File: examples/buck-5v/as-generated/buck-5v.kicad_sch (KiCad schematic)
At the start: 18 parts, among them J1 12V IN, J2 5V OUT, U1 LM2596S-5

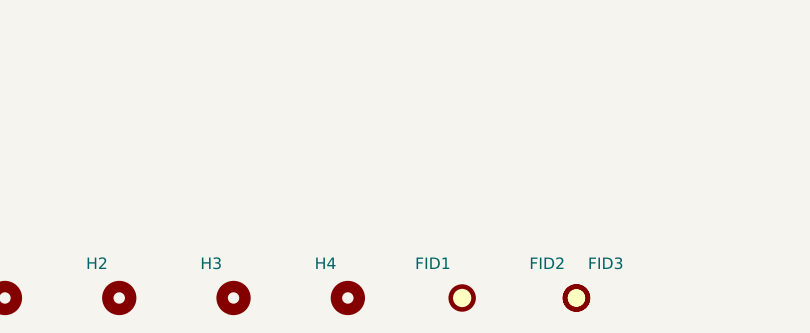
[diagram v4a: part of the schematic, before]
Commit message: Leave room for the screw, and print the ink where the board is
The screw holes were placed against the hole's own courtyard, which is the
drill plus a whisker - so on four of the five boards a hole sat inside a
connector's mating space, closest 0.42 mm. What goes through an M3 hole is a
pan head on a washer, seven millimetres of steel lying flat, and a connector
wants its shell, its wires and the fingers that fit them on top of that. The
spot search now keeps the fastener's own circle clear of every part body and
gives connectors CONNECTOR_ACCESS more, and three rules say so when a board
does not: mechanical.fastener_clearance, mechanical.connector_access and
mechanical.fastener_copper, all blocking for a generated design.

Silk was measured with a per-character advance of 0.78, and KiCad's stroke
font is proportional at 0.94 to 1.07. Everything downstream of that estimate
was placing ink where it did not fit: a legend across a capacitor's land, a
designator through the board's own name. `_text_extent` takes the top of the
measured range, adds the fab's clearance and is used by every silk placement.

Three placements also fell through to a position nobody chose. A designator
that found nothing kept its library offset, which for a part in a corner
points off the board; the board id took the first of eight fixed strips; a
legend took the least bad of six spots. All three are scored now, over
candidate sets wide enough to have an answer - and a pad-less footprint, which
is what a mounting hole is, is no longer skipped outright.

silk.off_board reports the case KiCad's own test cannot: ink that clears the
edge entirely is never printed, and DRC only measures ink that crosses it.

_unspiked redraws a corner tighter than a right angle as the elbow between its
neighbours - one diagonal, one straight, no step back to a heading the line
has already left. It is never longer than what it replaces.

All four fast boards: 0 errors, 0 warnings.

Co-Authored-By: Claude Fable 5 <no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
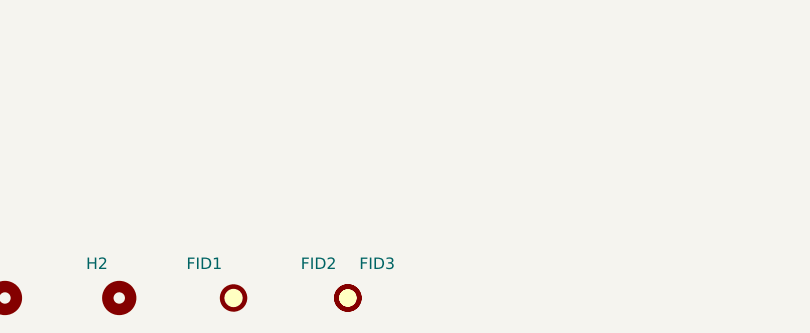
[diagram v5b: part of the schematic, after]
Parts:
- removed H3, H4: M3, MountingHole:MountingHole_3.2mm_M3, symbol Mechanical:MountingHole
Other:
- moved on the sheet: FID1, FID2, FID3
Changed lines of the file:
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@@
     (instances (project "buck-5v" (path "/ec98644d-848c-5056-a4cb-c829189be5c3" (reference "H2") (unit 1))))
   )
-  (symbol (lib_id "Mechanical:MountingHole") (at 51.11 149.67 0.0) (unit 1)
+  (symbol (lib_id "Mechanical:Fiducial") (at 51.11 149.67 0.0) (unit 1)
     (exclude_from_sim no) (in_bom no) (on_board yes) (dnp no)
-    (property "Reference" "H3" (at 49.84 145.86 0) (effects (font (size 1.27 1.27)) (justify right)))
-    (property "Value" "M3" (at 54.92 152.21 0) (effects (font (size 1.27 1.27)) (justify left) hide))
-    (property "Footprint" "MountingHole:MountingHole_3.2mm_M3" (at 51.11 149.67 0) (effects (font (size 1.27 1.27)) hide))
+    (property "Reference" "FID1" (at 49.84 145.86 0) (effects (font (size 1.27 1.27)) (justify right)))
+    (property "Value" "Fiducial" (at 54.92 152.21 0) (effects (font (size 1.27 1.27)) (justify left) hide))
+    (property "Footprint" "Fiducial:Fiducial_1mm_Mask2mm" (at 51.11 149.67 0) (effects (font (size 1.27 1.27)) hide))
     (property "Datasheet" "~" (at 51.11 149.67 0) (effects (font (size 1.27 1.27)) hide))
-    (instances (project "buck-5v" (path "/ec98644d-848c-5056-a4cb-c829189be5c3" (reference "H3") (unit 1))))
-  )
-  (symbol (lib_id "Mechanical:MountingHole") (at 63.81 149.67 0.0) (unit 1)
-    (exclude_from_sim no) (in_bom no) (on_board yes) (dnp no)
-    (property "Reference" "H4" (at 62.54 145.86 0) (effects (font (size 1.27 1.27)) (justify right)))
-    (property "Value" "M3" (at 67.62 152.21 0) (effects (font (size 1.27 1.27)) (justify left) hide))
-    (property "Footprint" "MountingHole:MountingHole_3.2mm_M3" (at 63.81 149.67 0) (effects (font (size 1.27 1.27)) hide))
-    (property "Datasheet" "~" (at 63.81 149.67 0) (effects (font (size 1.27 1.27)) hide))
-    (instances (project "buck-5v" (path "/ec98644d-848c-5056-a4cb-c829189be5c3" (reference "H4") (unit 1))))
-  )
-  (symbol (lib_id "Mechanical:Fiducial") (at 76.51 149.67 0.0) (unit 1)
-    (exclude_from_sim no) (in_bom no) (on_board yes) (dnp no)
-    (property "Reference" "FID1" (at 75.24 145.86 0) (effects (font (size 1.27 1.27)) (justify right)))
-    (property "Value" "Fiducial" (at 80.32 152.21 0) (effects (font (size 1.27 1.27)) (justify left) hide))
-    (property "Footprint" "Fiducial:Fiducial_1mm_Mask2mm" (at 76.51 149.67 0) (effects (font (size 1.27 1.27)) hide))
-    (property "Datasheet" "~" (at 76.51 149.67 0) (effects (font (size 1.27 1.27)) hide))
     (instances (project "buck-5v" (path "/ec98644d-848c-5056-a4cb-c829189be5c3" (reference "FID1") (unit 1))))
   )
-  (symbol (lib_id "Mechanical:Fiducial") (at 89.21 149.67 0.0) (unit 1)
+  (symbol (lib_id "Mechanical:Fiducial") (at 63.81 149.67 0.0) (unit 1)
     (exclude_from_sim no) (in_bom no) (on_board yes) (dnp no)
-    (property "Reference" "FID2" (at 87.94 145.86 0) (effects (font (size 1.27 1.27)) (justify right)))
-    (property "Value" "Fiducial" (at 93.02 152.21 0) (effects (font (size 1.27 1.27)) (justify left) hide))
-    (property "Footprint" "Fiducial:Fiducial_1mm_Mask2mm" (at 89.21 149.67 0) (effects (font (size 1.27 1.27)) hide))
-    (property "Datasheet" "~" (at 89.21 149.67 0) (effects (font (size 1.27 1.27)) hide))
+    (property "Reference" "FID2" (at 62.54 145.86 0) (effects (font (size 1.27 1.27)) (justify right)))
+    (property "Value" "Fiducial" (at 67.62 152.21 0) (effects (font (size 1.27 1.27)) (justify left) hide))
+    (property "Footprint" "Fiducial:Fiducial_1mm_Mask2mm" (at 63.81 149.67 0) (effects (font (size 1.27 1.27)) hide))
+    (property "Datasheet" "~" (at 63.81 149.67 0) (effects (font (size 1.27 1.27)) hide))
     (instances (project "buck-5v" (path "/ec98644d-848c-5056-a4cb-c829189be5c3" (reference "FID2") (unit 1))))
   )
-  (symbol (lib_id "Mechanical:Fiducial") (at 89.21 149.67 0.0) (unit 1)
+  (symbol (lib_id "Mechanical:Fiducial") (at 63.81 149.67 0.0) (unit 1)
     (exclude_from_sim no) (in_bom no) (on_board yes) (dnp no)
-    (property "Reference" "FID3" (at 90.48 145.86 0) (effects (font (size 1.27 1.27)) (justify left)))
-    (property "Value" "Fiducial" (at 90.48 154.75 0) (effects (font (size 1.27 1.27)) (justify left) hide))
-    (property "Footprint" "Fiducial:Fiducial_1mm_Mask2mm" (at 89.21 149.67 0) (effects (font (size 1.27 1.27)) hide))
-    (property "Datasheet" "~" (at 89.21 149.67 0) (effects (font (size 1.27 1.27)) hide))
+    (property "Reference" "FID3" (at 65.08 145.86 0) (effects (font (size 1.27 1.27)) (justify left)))
+    (property "Value" "Fiducial" (at 65.08 154.75 0) (effects (font (size 1.27 1.27)) (justify left) hide))
+    (property "Footprint" "Fiducial:Fiducial_1mm_Mask2mm" (at 63.81 149.67 0) (effects (font (size 1.27 1.27)) hide))
+    (property "Datasheet" "~" (at 63.81 149.67 0) (effects (font (size 1.27 1.27)) hide))
     (instances (project "buck-5v" (path "/ec98644d-848c-5056-a4cb-c829189be5c3" (reference "FID3") (unit 1))))
   )

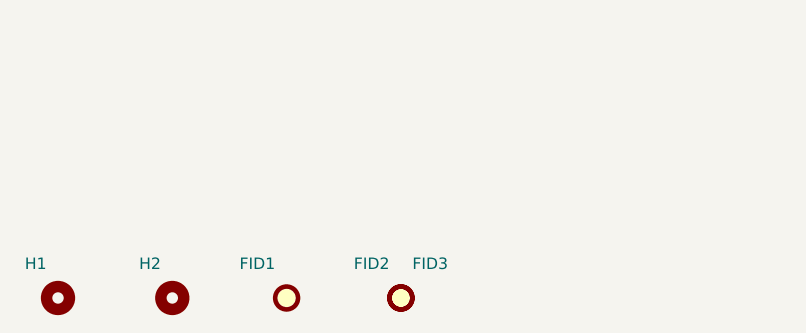
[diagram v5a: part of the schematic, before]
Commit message: Walk the whole edge for a screw hole, and land a joint on its own pad
The fastener clearance was right and the search was not: it slid along two
edges from each corner and gave up, so boards that had had four screw holes
came back with one. It now walks a ring round the board at the inset the
screw needs, taking the nearest free point to each corner - and only from
that corner's own quarter, because a search that asked for the nearest free
point anywhere put three of the four along one edge, each of them the nearest
thing to a different corner. A quarter with no room gives no screw: three
that hold the board flat beat four that hold one side.

A pin header asks for nothing above its courtyard - the socket that fits it
lands inside the outline the header already draws - while a screw terminal's
wires leave horizontally from its face. Treating the two alike is what left a
carrier lined with headers with two holes on one edge. Both the generator and
the rule now tell them apart by footprint.

_landed folds a via that sits beside a plated hole of its own net onto the
hole. The plating already joins the faces, so the via bought nothing and cost
hole-to-hole: two drills a millimetre apart leave 0.15 mm of laminate at a
0.25 mm rule, which is what DRC reported on the opamp board.

The fillets move to the end of the pipeline. A taper is built against the end
of a run, and _landed moves ends, so a teardrop laid before it pointed at
where the run used to stop - a nought-degree corner in the angle rule.

buck-5v, motor-driver, pico-carrier, opamp-filter: 0 errors, 0 warnings.

Co-Authored-By: Claude Fable 5 <noreply@anthropic.com>
Claude-Session: https://claude.ai/code/session_01DUj7Ltu92tWg159mCSacwY
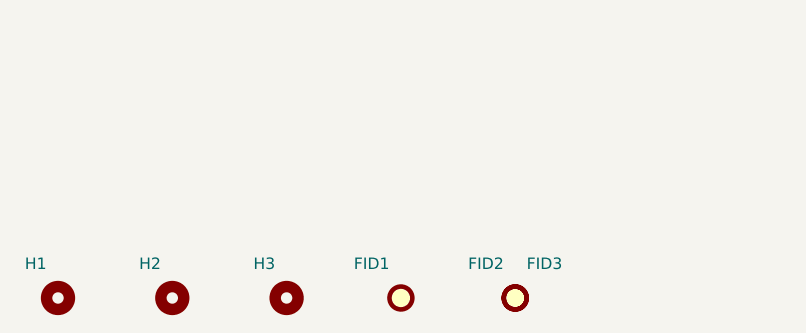
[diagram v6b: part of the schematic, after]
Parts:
- added H3: M3, MountingHole:MountingHole_3.2mm_M3, symbol Mechanical:MountingHole
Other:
- moved on the sheet: FID1, FID2, FID3
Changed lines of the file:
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@@
     (instances (project "buck-5v" (path "/ec98644d-848c-5056-a4cb-c829189be5c3" (reference "H2") (unit 1))))
   )
-  (symbol (lib_id "Mechanical:Fiducial") (at 51.11 149.67 0.0) (unit 1)
+  (symbol (lib_id "Mechanical:MountingHole") (at 51.11 149.67 0.0) (unit 1)
     (exclude_from_sim no) (in_bom no) (on_board yes) (dnp no)
-    (property "Reference" "FID1" (at 49.84 145.86 0) (effects (font (size 1.27 1.27)) (justify right)))
-    (property "Value" "Fiducial" (at 54.92 152.21 0) (effects (font (size 1.27 1.27)) (justify left) hide))
-    (property "Footprint" "Fiducial:Fiducial_1mm_Mask2mm" (at 51.11 149.67 0) (effects (font (size 1.27 1.27)) hide))
+    (property "Reference" "H3" (at 49.84 145.86 0) (effects (font (size 1.27 1.27)) (justify right)))
+    (property "Value" "M3" (at 54.92 152.21 0) (effects (font (size 1.27 1.27)) (justify left) hide))
+    (property "Footprint" "MountingHole:MountingHole_3.2mm_M3" (at 51.11 149.67 0) (effects (font (size 1.27 1.27)) hide))
     (property "Datasheet" "~" (at 51.11 149.67 0) (effects (font (size 1.27 1.27)) hide))
-    (instances (project "buck-5v" (path "/ec98644d-848c-5056-a4cb-c829189be5c3" (reference "FID1") (unit 1))))
+    (instances (project "buck-5v" (path "/ec98644d-848c-5056-a4cb-c829189be5c3" (reference "H3") (unit 1))))
   )
   (symbol (lib_id "Mechanical:Fiducial") (at 63.81 149.67 0.0) (unit 1)
     (exclude_from_sim no) (in_bom no) (on_board yes) (dnp no)
-    (property "Reference" "FID2" (at 62.54 145.86 0) (effects (font (size 1.27 1.27)) (justify right)))
+    (property "Reference" "FID1" (at 62.54 145.86 0) (effects (font (size 1.27 1.27)) (justify right)))
     (property "Value" "Fiducial" (at 67.62 152.21 0) (effects (font (size 1.27 1.27)) (justify left) hide))
     (property "Footprint" "Fiducial:Fiducial_1mm_Mask2mm" (at 63.81 149.67 0) (effects (font (size 1.27 1.27)) hide))
     (property "Datasheet" "~" (at 63.81 149.67 0) (effects (font (size 1.27 1.27)) hide))
+    (instances (project "buck-5v" (path "/ec98644d-848c-5056-a4cb-c829189be5c3" (reference "FID1") (unit 1))))
+  )
+  (symbol (lib_id "Mechanical:Fiducial") (at 76.51 149.67 0.0) (unit 1)
+    (exclude_from_sim no) (in_bom no) (on_board yes) (dnp no)
+    (property "Reference" "FID2" (at 75.24 145.86 0) (effects (font (size 1.27 1.27)) (justify right)))
+    (property "Value" "Fiducial" (at 80.32 152.21 0) (effects (font (size 1.27 1.27)) (justify left) hide))
+    (property "Footprint" "Fiducial:Fiducial_1mm_Mask2mm" (at 76.51 149.67 0) (effects (font (size 1.27 1.27)) hide))
+    (property "Datasheet" "~" (at 76.51 149.67 0) (effects (font (size 1.27 1.27)) hide))
     (instances (project "buck-5v" (path "/ec98644d-848c-5056-a4cb-c829189be5c3" (reference "FID2") (unit 1))))
   )
-  (symbol (lib_id "Mechanical:Fiducial") (at 63.81 149.67 0.0) (unit 1)
+  (symbol (lib_id "Mechanical:Fiducial") (at 76.51 149.67 0.0) (unit 1)
     (exclude_from_sim no) (in_bom no) (on_board yes) (dnp no)
-    (property "Reference" "FID3" (at 65.08 145.86 0) (effects (font (size 1.27 1.27)) (justify left)))
-    (property "Value" "Fiducial" (at 65.08 154.75 0) (effects (font (size 1.27 1.27)) (justify left) hide))
-    (property "Footprint" "Fiducial:Fiducial_1mm_Mask2mm" (at 63.81 149.67 0) (effects (font (size 1.27 1.27)) hide))
-    (property "Datasheet" "~" (at 63.81 149.67 0) (effects (font (size 1.27 1.27)) hide))
+    (property "Reference" "FID3" (at 77.78 145.86 0) (effects (font (size 1.27 1.27)) (justify left)))
+    (property "Value" "Fiducial" (at 77.78 154.75 0) (effects (font (size 1.27 1.27)) (justify left) hide))
+    (property "Footprint" "Fiducial:Fiducial_1mm_Mask2mm" (at 76.51 149.67 0) (effects (font (size 1.27 1.27)) hide))
+    (property "Datasheet" "~" (at 76.51 149.67 0) (effects (font (size 1.27 1.27)) hide))
     (instances (project "buck-5v" (path "/ec98644d-848c-5056-a4cb-c829189be5c3" (reference "FID3") (unit 1))))
   )

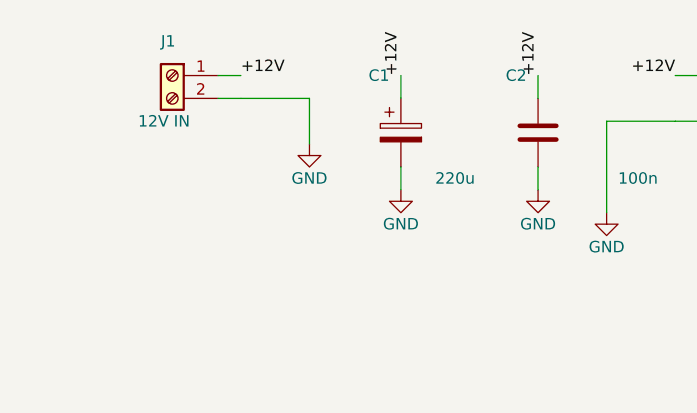
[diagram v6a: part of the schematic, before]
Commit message: feat(examples): round twenty - fuse and clamp every input, state the ESR, damp the clock, control the mute
Redesign of the five worked examples for the items REVIEW.md left open:

- every power input gets a fuse in series and a TVS across the fused rail
  (a resettable fuse on the Pico carrier, whose Schottky already blocks a
  reversed supply); each sheet states what the clamp does not do
- the buck's output capacitor states the ESR the LM2596 loop is designed
  around (SNVS124G 9.1.3), derived from the ripple already on the sheet
- the FPGA's 12 MHz clock leaves its oscillator through 33 ohms
- the DAC's XSMT is driven from the FPGA with a pull-down instead of
  strapped high, so it comes up muted
- the op-amp filter's output goes through a 100 ohm isolation resistor

Generator fixes the round found: _surfaced pruned a via that tapped the
middle of a back-layer spine, and _chamfer_tracks cut the copper out from
under a via sitting a fraction along a leg; both left a net in two pieces
that KiCad's DRC reported. Pin stubs closer than 7.62 mm draw over each
other, so the new parts are spaced for it and the comments say why.

tools/example_images.py renders the README pictures from the regenerated
projects. All five reviewed variants pass their gates and KiCad's DRC on
both matrix versions; the as-generated variants each carry one more
blocking finding (spec.missing_esr). REVIEW.md 25 records the round.

Co-Authored-By: Claude Fable 5.1 <noreply@anthropic.com>
Claude-Session: https://claude.ai/code/session_017JKofiLFxXjzRRnBmFyXuQ
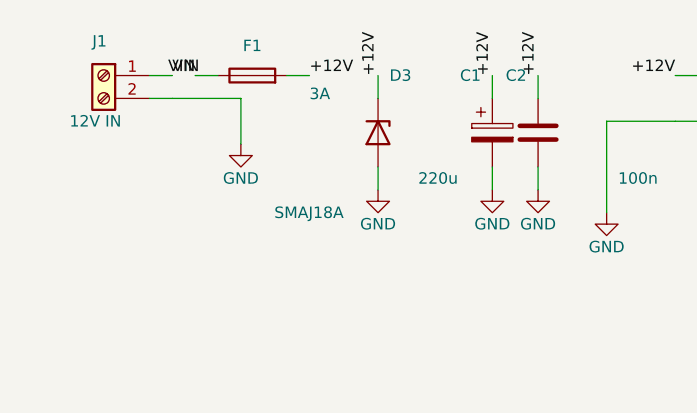
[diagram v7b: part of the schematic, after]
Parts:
- added D3: SMAJ18A, Diode_SMD:D_SMA, symbol Device:D_Zener
- added F1: 3A, Fuse:Fuse_1206_3216Metric, symbol Device:Fuse
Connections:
- net +12V: now also D3.1 (K), F1.2; no longer J1.1 (Pin_1)
- net GND: now also D3.2 (A)
- new net VIN: F1.1, J1.1 (Pin_1)
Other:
- moved on the sheet: C1, J1
